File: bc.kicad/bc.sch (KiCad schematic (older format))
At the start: 68 parts, among them J1 Edge Connector, Q1 PMV48XP, SW1 SW_Push, U1 STM32L052C8Tx

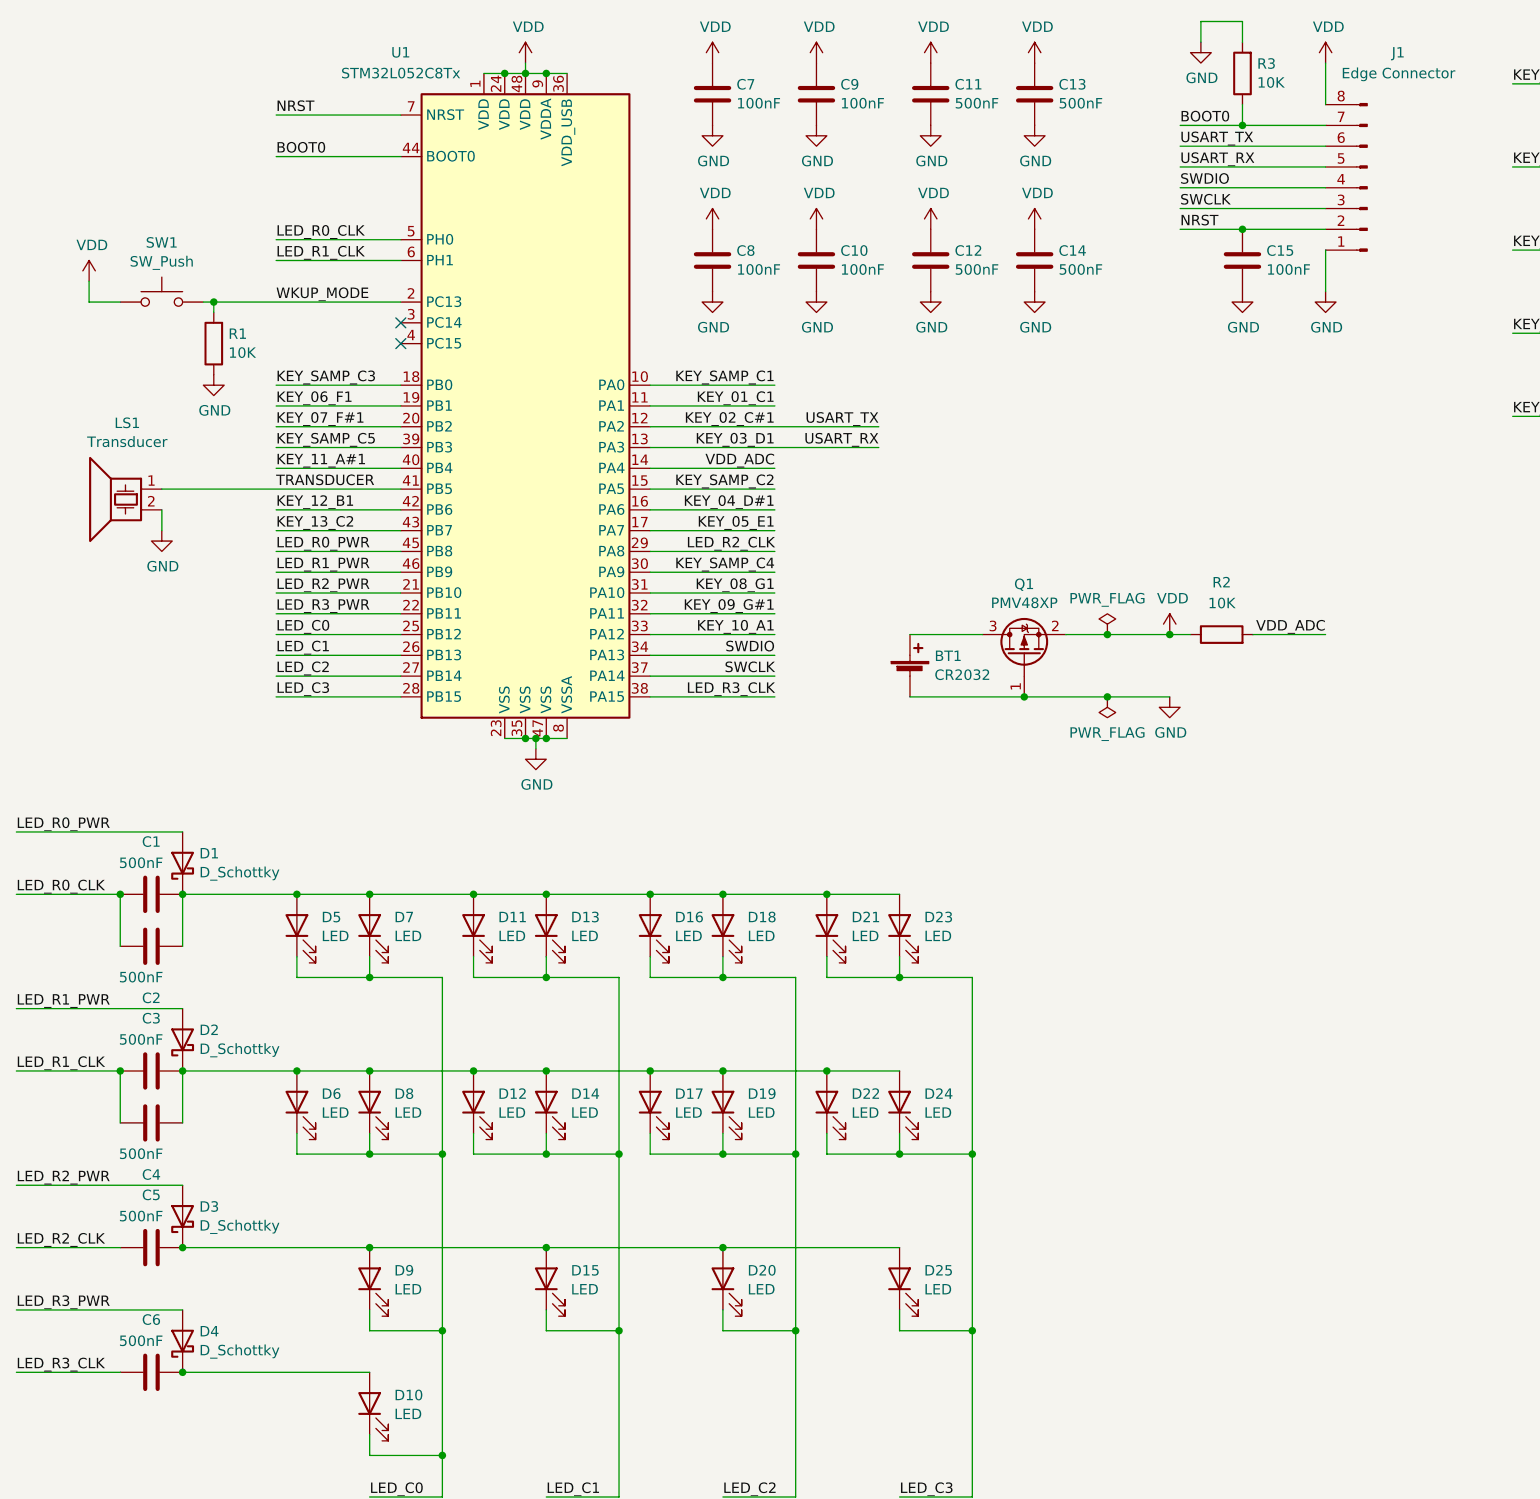
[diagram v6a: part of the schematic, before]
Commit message: Define some parts and footprints
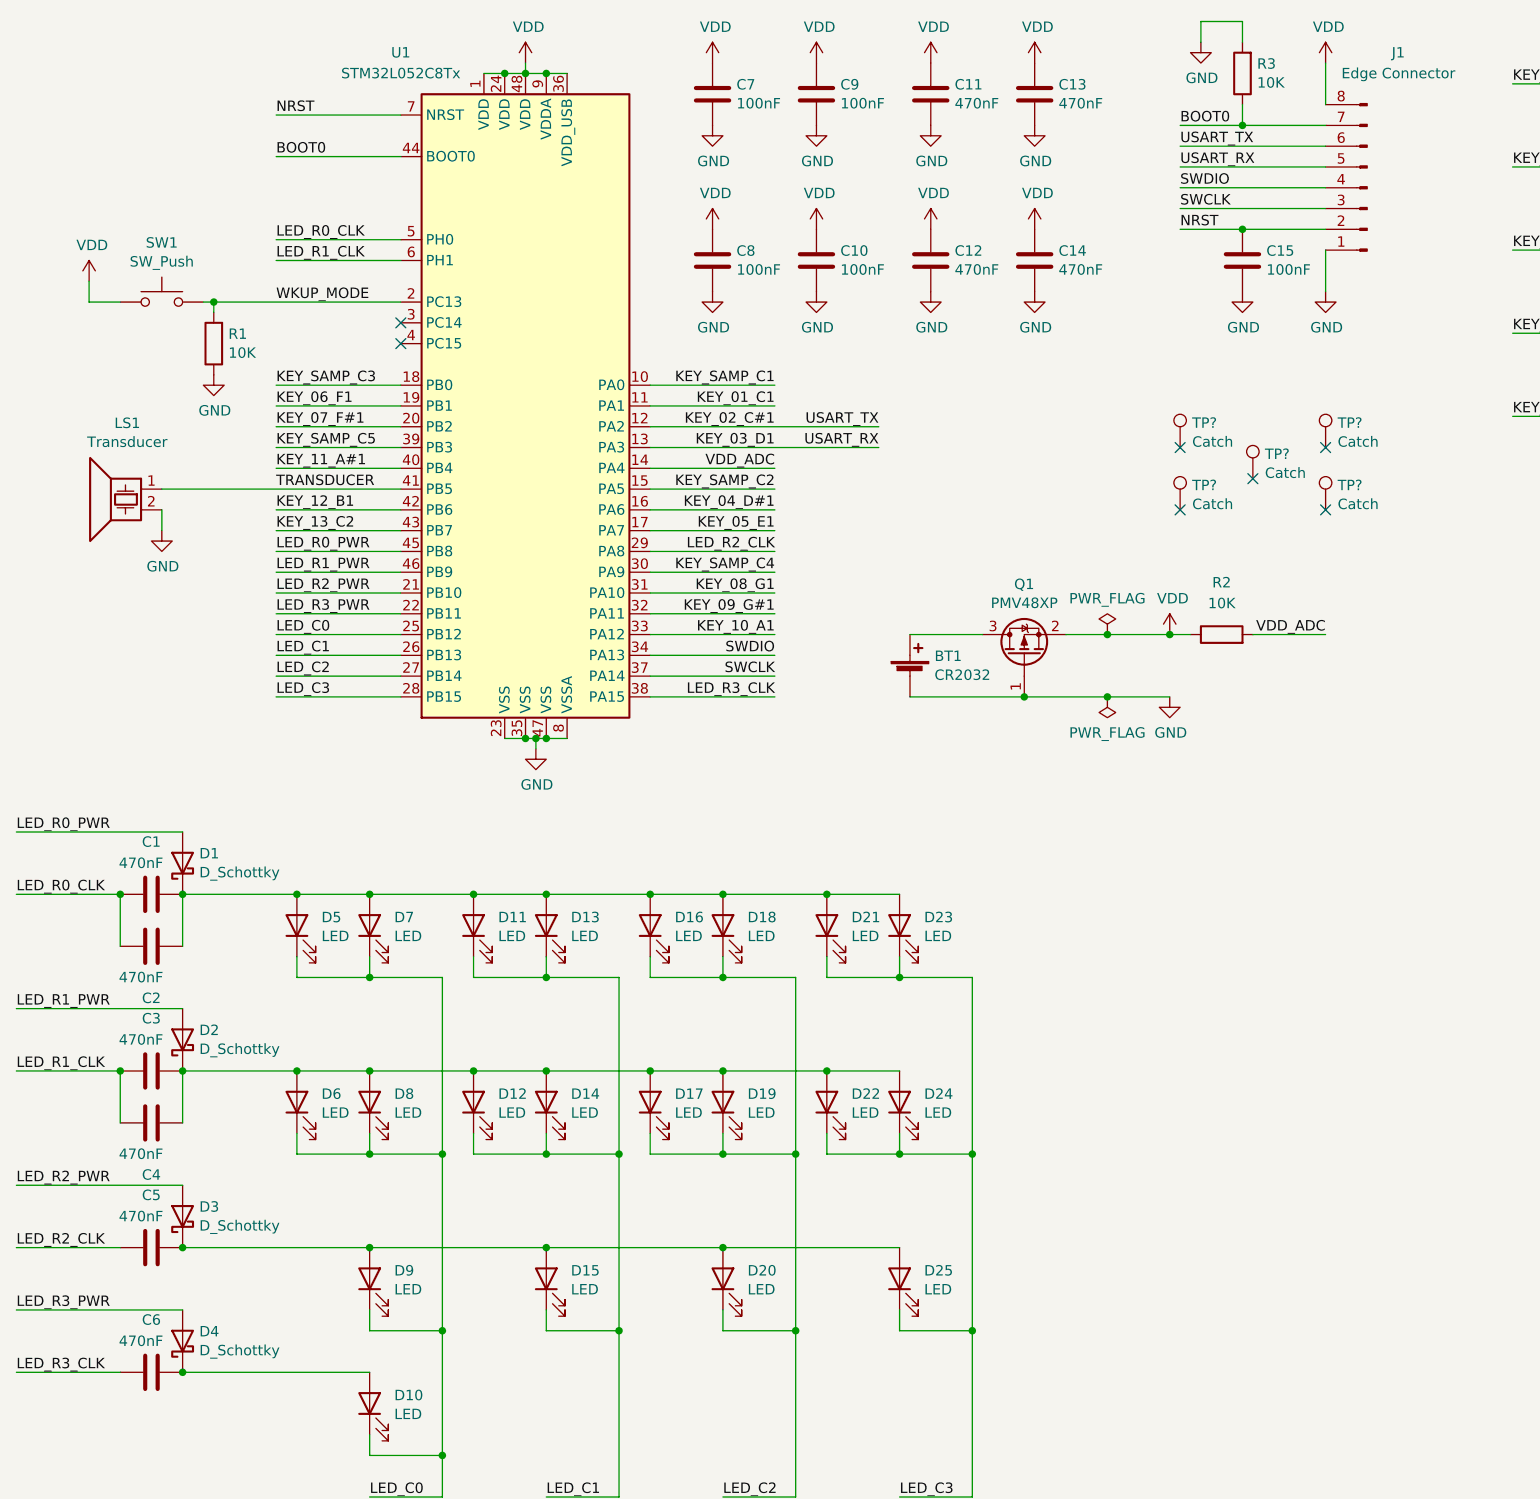
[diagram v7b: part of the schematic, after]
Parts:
- added TP? (x5): Catch, symbol Connector:TestPoint
- BT1: LCSC (none) -> C238099
- C1, C11, C12, C13, C14, C2, C3, C4, C5, C6: value 500nF -> 470nF; footprint (none) -> Capacitor_SMD:C_0603_1608Metric; LCSC (none) -> C1623
- C10, C15, C16, C17, C18, C19, C20, C7, C8, C9: footprint (none) -> Capacitor_SMD:C_0603_1608Metric; LCSC (none) -> C14663
- D1, D2, D3, D4: footprint (none) -> Diode_SMD:D_SOD-123; LCSC (none) -> C8598
- Q1: footprint (none) -> Package_TO_SOT_SMD:SOT-23
- R1, R10, R11, R12, R13, R14, R15, R16, R2, R3, R4, R5, R6, R7, R8, R9: footprint (none) -> Resistor_SMD:R_0603_1608Metric; LCSC (none) -> C25804
- SW1: LCSC (none) -> C318889
- U1: LCSC (none) -> C111213
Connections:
- no-connect marks 2 -> 7

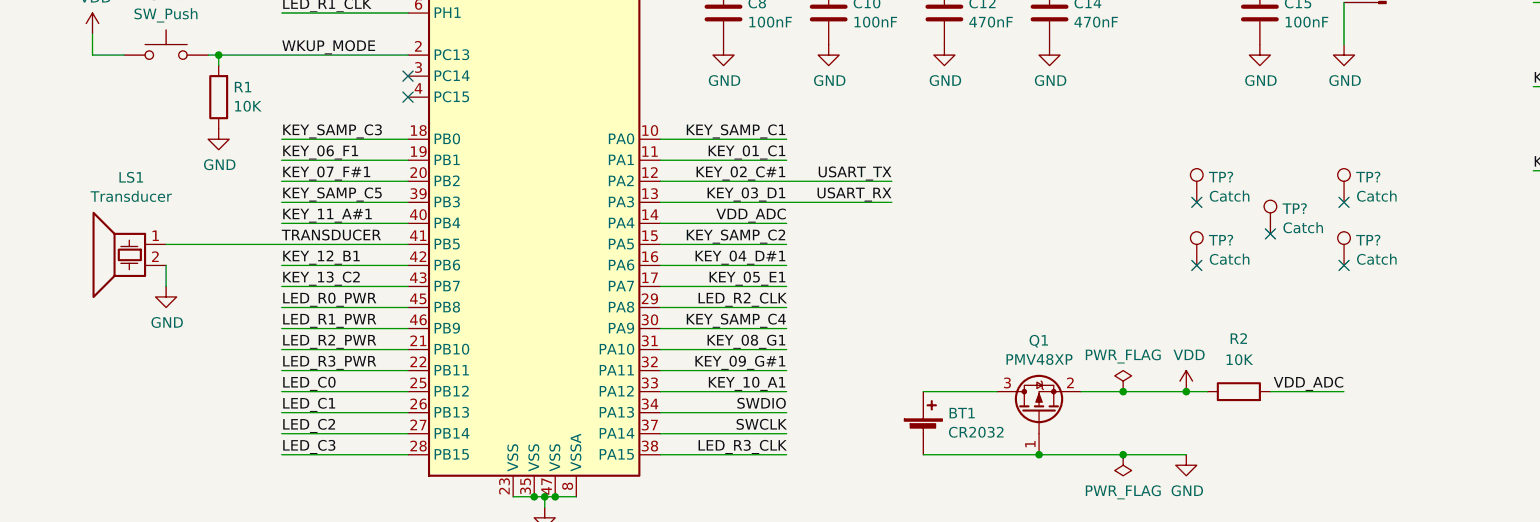
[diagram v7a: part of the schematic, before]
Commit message: Assign all parts/footprints except keyboard
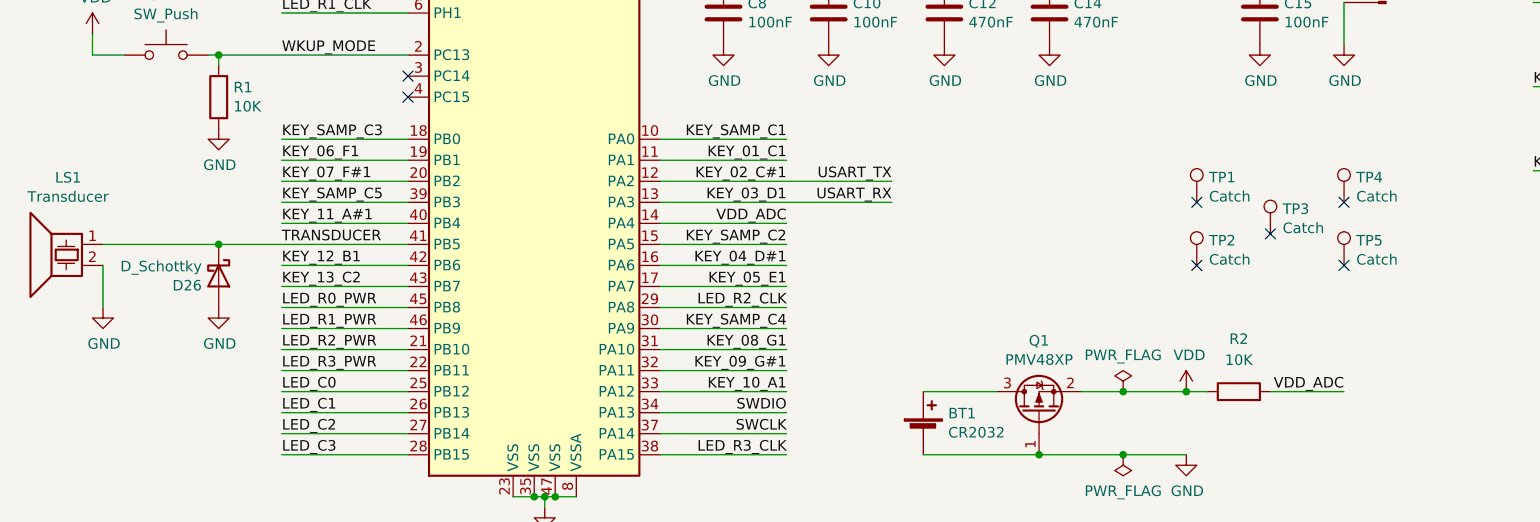
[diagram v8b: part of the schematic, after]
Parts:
- added D26: D_Schottky, Diode_SMD:D_SOD-123, symbol Device:D_Schottky
- D10, D11, D12, D13, D14, D15, D16, D17, D18, D19, D20, D21, D22, D23, D24, D25, D6, D7, D8, D9: footprint (none) -> bc:side_led
- D5: footprint (none) -> bc:side_led; Digi-Key (none) -> 160-1870-1-ND
- J1: footprint (none) -> bc:edge_connector
- LS1: footprint (none) -> bc:transducer; Digi-Key (none) -> 668-1538-1-ND
- SW1: footprint (none) -> bc:SW_Push_1P1T_NO_5.1x5.1mm_H2.5mm
- TP1, TP2, TP3, TP4, TP5: renamed from TP?; footprint (none) -> bc:test_point
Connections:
- net GND: now also D26.2 (A)
- net TRANSDUCER: now also D26.1 (K)
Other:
- moved on the sheet: LS1
